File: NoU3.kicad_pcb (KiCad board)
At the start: 4 copper layers, 46 x 56 mm, 119 parts, among them J1 JST SR/SZ, J10 JST SR/SZ, J11 Screw_Terminal_01x02, J12 Screw_Terminal_01x02, J13 JST SR/SZ, J14 RFANT3216120A5T, J15 Barrel_Jack, J16 VIN, J17 JST SR/SZ, J18 GND, J19 JST SR/SZ, J2 Screw_Terminal_01x02, J3 Screw_Terminal_01x02, J4 JST SR/SZ, J5 Screw_Terminal_01x02, J6 Screw_Terminal_01x02, J7 JST SR/SZ, J8 Screw_Terminal_01x02, J9 Screw_Terminal_01x02, Q1 AO3401A, SW1 reset, SW2 boot, U1 HR8833, U10 PCA9685BS, U11 Qwiic1, U15 SY8113BADC, U16 SY8113BADC, U17 USB_C_Receptacle, U18 ServoPorts_2x3, U19 ServoPorts_2x3, U2 ESP32-S3FN8, U26 LSM6DS3TR-C, U3 Crystal_ESP32, U4 HR8833, U5 HR8833, U6 HR8833, U7 ServoPorts_2x3, U8 5.8 ZSPT, U9 USBLC6-2P6

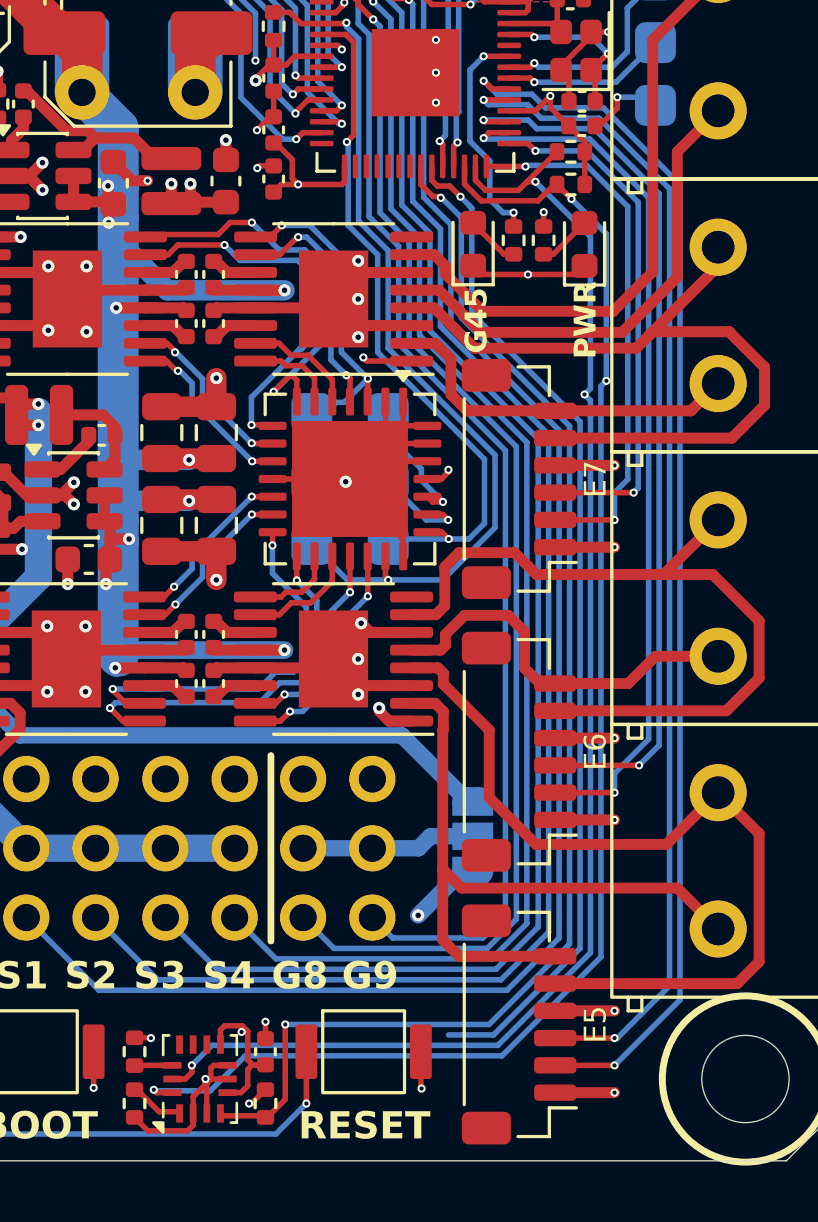
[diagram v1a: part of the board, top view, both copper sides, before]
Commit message: cleaned up JSTs on motor driver sheet
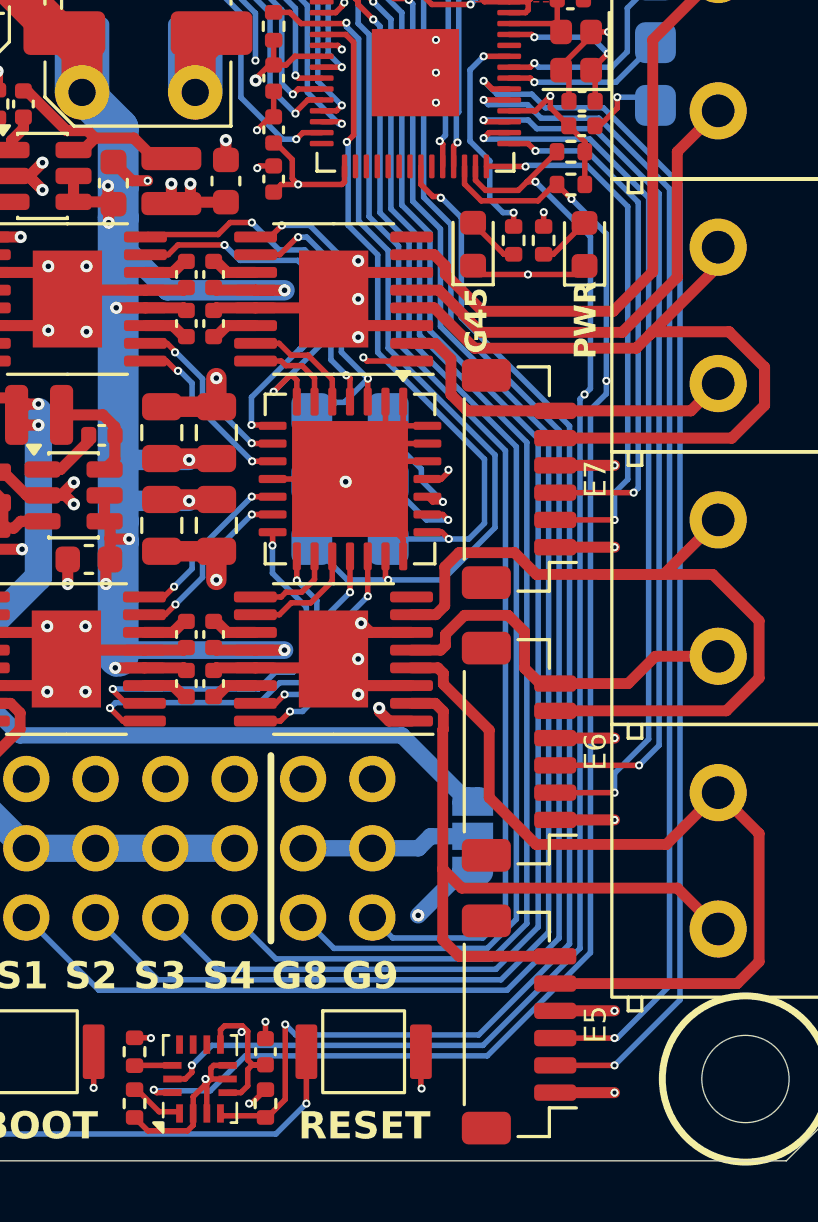
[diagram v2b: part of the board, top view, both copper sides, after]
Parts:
- C1: value 100nF -> 1uF
- R5: value 1K -> 10K
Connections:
- net /MotorSystem/MotorDriver-1/Aout1 renamed Net-(J1-Pin_6)
- net /MotorSystem/MotorDriver-1/Aout2 renamed Net-(J1-Pin_5)
- net /MotorSystem/MotorDriver-3/Aout1 renamed Net-(J7-Pin_6)
- net /MotorSystem/MotorDriver-3/Aout2 renamed Net-(J7-Pin_5)
- net /MotorSystem/MotorDriver-4/Aout1 renamed Net-(J10-Pin_6)
- net /MotorSystem/MotorDriver-4/Aout2 renamed Net-(J10-Pin_5)
- net MD2_A1 renamed Net-(J19-Pin_6)
- net MD2_A2 renamed Net-(J19-Pin_5)
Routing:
- net SF_INT1: track 37.3 -> 0.00 mm, vias 1 -> 0

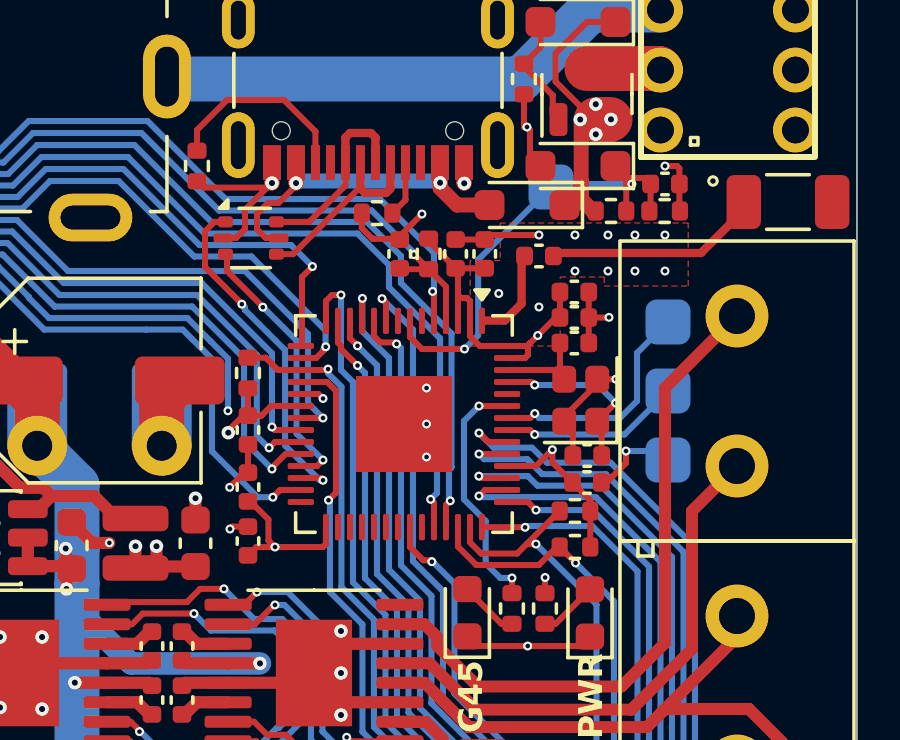
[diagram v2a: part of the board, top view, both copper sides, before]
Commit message: Reroute PCB connections and adjust DRC rules
Add and revise PCB routing for several connector and component nets, including repositioning U9. Ignore silkscreen clearance and overlap violations, and update schematic notes.
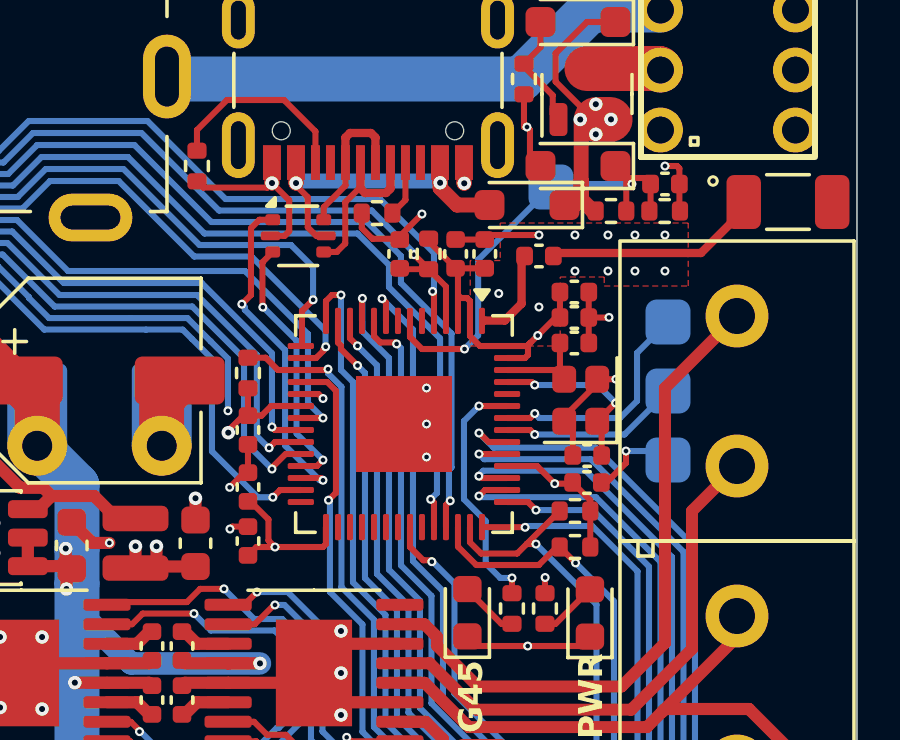
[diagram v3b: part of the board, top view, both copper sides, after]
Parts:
- moved U9 1.58 mm to (4.38, -16.2)
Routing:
- net Net-(U17-D+-PadA6): track 6.36 -> 5.00 mm
- net Net-(U17-D--PadA7): track 6.56 -> 5.73 mm
- net /VUSB: track 11.4 -> 10.6 mm
- net +3V3: track 64.3 -> 63.7 mm

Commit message: first push with NoU3.7 features
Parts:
- removed Q1: AO3401A, AlfredoFootprints:SOT-23-small
- removed R23: 10K, Resistor_SMD:R_0402_1005Metric
- removed TP4: ECLK, AlfredoFootprints:PogoPad1
- removed TP5: LED0, AlfredoFootprints:PogoPad1
- removed TP6: SCL, AlfredoFootprints:PogoPad1
- removed TP7: SDA, AlfredoFootprints:PogoPad1
- removed TP8: MOE, AlfredoFootprints:PogoPad1
- removed TP9: GND, AlfredoFootprints:PogoPad1
- removed U10: PCA9685BS, Package_DFN_QFN:QFN-28-1EP_6x6mm_P0.65mm_EP4.25x4.25mm
- added C17: 100nF, Capacitor_SMD:C_0402_1005Metric, F.Cu at (-17.3, -35.7)
- added C18: 100nF, Capacitor_SMD:C_0402_1005Metric, F.Cu at (-17.3, -33.7)
- added C39: 10uF, Capacitor_SMD:C_0402_1005Metric, F.Cu at (-17.3, -31.8)
- added D60: LED_yellow, LED_SMD:LED_0402_1005Metric, F.Cu at (-14.1, -35.7)
- added J20: JST SR/SZ, AlfredoFootprints:JST_SH_1x06_Vertical, F.Cu at (-13.3, -41.8)
- added Q2: AONR21357, Package_DFN_QFN:DFN-8-1EP_3x3mm_P0.65mm_EP1.55x2.4mm, F.Cu at (-31.4, -44.4)
- added R29: 100mR, Resistor_SMD:R_0805_2012Metric, F.Cu at (-36.9, -36.0)
- added R30: 100mR, Resistor_SMD:R_0805_2012Metric, F.Cu at (-24.1, -36.0)
- added R31: 100mR, Resistor_SMD:R_0805_2012Metric, F.Cu at (-36.9, -28.1)
- added R32: 100mR, Resistor_SMD:R_0805_2012Metric, F.Cu at (-30.5, -36.0)
- added R33: 100mR, Resistor_SMD:R_0805_2012Metric, F.Cu at (-36.9, -33.0)
- added R34: 100mR, Resistor_SMD:R_0805_2012Metric, F.Cu at (-24.1, -33.0)
- added R35: 100mR, Resistor_SMD:R_0805_2012Metric, F.Cu at (-36.4, -24.1)
- added R36: 100mR, Resistor_SMD:R_0805_2012Metric, F.Cu at (-30.5, -33.0)
- added R67: 1K, Resistor_SMD:R_0201_0603Metric, F.Cu at (-14.6, -33.8)
- added U12: PY32F003F16U6TR, Package_DFN_QFN:VQFN-20-1EP_3x3mm_P0.4mm_EP1.7x1.7mm, F.Cu at (-29.7, -26.9)
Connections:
- net /MotorSystem/MotorDriver-1/Bout1 renamed Net-(J20-Pin_6)
- net /MotorSystem/MotorDriver-1/Bout2 renamed Net-(J20-Pin_5)
- J10 pad 2: E4B -> E6A
- J12 pad 1: MD4_B1 -> Net-(J12-Pin_1)
- J12 pad 2: MD4_B2 -> Net-(J12-Pin_2)
- J13 pad 3: E5A -> E3B
- J13 pad 5: MD3_B1 -> Net-(J13-Pin_5)
- J13 pad 6: MD3_B2 -> Net-(J13-Pin_6)
- J17 pad 3: E6A -> E4B
- J17 pad 5: MD4_B1 -> Net-(J12-Pin_2)
- J17 pad 6: MD4_B2 -> Net-(J12-Pin_1)
- J19 pad 2: E7B -> E2A
- J4 pad 3: E2A -> E7B
- J4 pad 5: /MotorSystem/MotorDriver-2/Bout1 -> Net-(J4-Pin_5)
- J4 pad 6: /MotorSystem/MotorDriver-2/Bout2 -> Net-(J4-Pin_6)
- J6 pad 1: /MotorSystem/MotorDriver-2/Bout1 -> Net-(J4-Pin_6)
- J6 pad 2: /MotorSystem/MotorDriver-2/Bout2 -> Net-(J4-Pin_5)
- J7 pad 2: E3B -> E5A
- J9 pad 1: MD3_B1 -> Net-(J13-Pin_6)
- J9 pad 2: MD3_B2 -> Net-(J13-Pin_5)
- U1 pad 3: GND -> /MotorSystem/MotorDriver-1/AISEN
- U1 pad 6: GND -> /MotorSystem/MotorDriver-1/BISEN
- U4 pad 3: GND -> /MotorSystem/MotorDriver-2/AISEN
- U4 pad 5: /MotorSystem/MotorDriver-2/Bout2 -> Net-(J4-Pin_5)
- U4 pad 6: GND -> /MotorSystem/MotorDriver-2/BISEN
- U4 pad 7: /MotorSystem/MotorDriver-2/Bout1 -> Net-(J4-Pin_6)
- U5 pad 3: GND -> /MotorSystem/MotorDriver-3/AISEN
- U5 pad 5: MD3_B2 -> Net-(J13-Pin_5)
- U5 pad 6: GND -> /MotorSystem/MotorDriver-3/BISEN
- U5 pad 7: MD3_B1 -> Net-(J13-Pin_6)
- U6 pad 3: GND -> /MotorSystem/MotorDriver-4/AISEN
- U6 pad 5: MD4_B2 -> Net-(J12-Pin_2)
- U6 pad 6: GND -> /MotorSystem/MotorDriver-4/BISEN
- U6 pad 7: MD4_B1 -> Net-(J12-Pin_1)
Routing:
- net (no net): track 0.00 -> 146.0 mm, vias 0 -> 2
- net MD4_B1: track 30.8 -> 0.00 mm
- net /MotorSystem/MotorDriver-2/Bout2: track 28.8 -> 0.00 mm
- net MD3_B2: track 28.1 -> 0.00 mm, vias 2 -> 0
- net MD3_B1: track 25.6 -> 0.00 mm
- net GND: track 148.6 -> 128.2 mm, vias 68 -> 67
- net /MotorSystem/MotorDriver-2/Bout1: track 17.8 -> 0.00 mm
- net MD4_B2: track 14.9 -> 0.00 mm
- net /MotorSystem/MotorDriver-2/AIN1: track 14.6 -> 0.00 mm, vias 2 -> 0
- net /MotorSystem/MotorDriver-3/BIN2: track 14.1 -> 0.00 mm, vias 2 -> 0
- net /MotorSystem/MotorDriver-3/BIN1: track 14.0 -> 0.00 mm, vias 2 -> 0
- net /MotorSystem/MotorDriver-2/AIN2: track 13.9 -> 0.00 mm, vias 2 -> 0
- net /MotorSystem/MotorDriver-1/BIN1: track 12.1 -> 0.00 mm, vias 2 -> 0
- net VCC: track 120.2 -> 110.2 mm, vias 14 -> 10
- net /MotorSystem/MotorDriver-1/BIN2: track 8.67 -> 0.00 mm, vias 2 -> 0
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
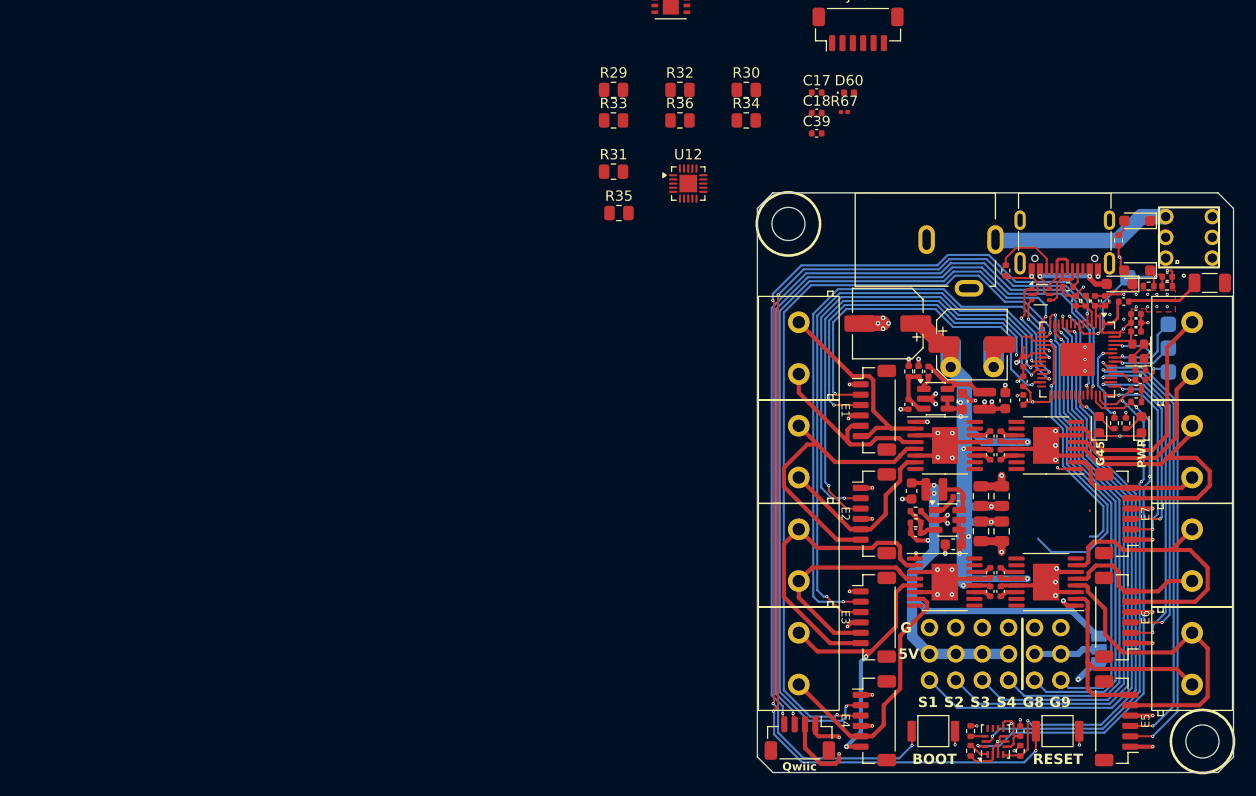
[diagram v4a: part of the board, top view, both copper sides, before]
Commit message: PY32F030K28U6TR motor controller chip
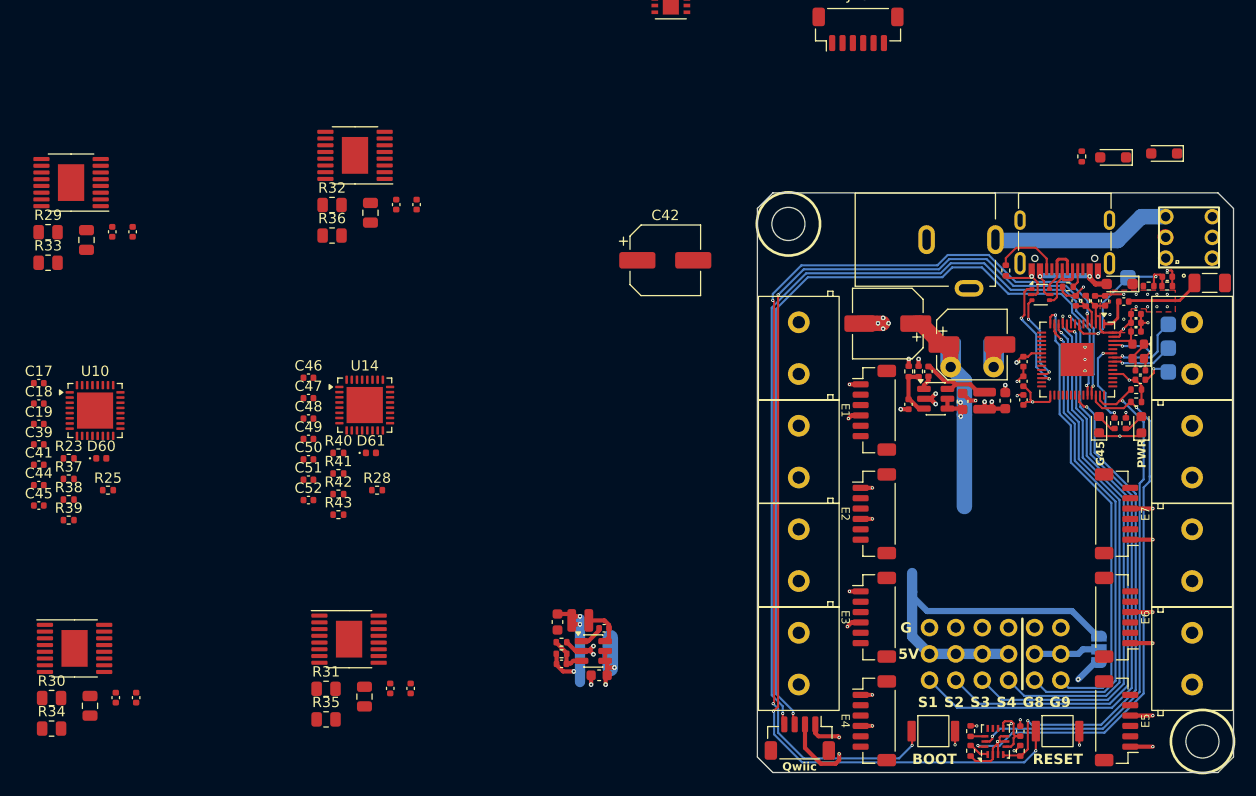
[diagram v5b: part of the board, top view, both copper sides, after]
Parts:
- removed R67: 1K, Resistor_SMD:R_0201_0603Metric
- removed U12: PY32F003F16U6TR, Package_DFN_QFN:VQFN-20-1EP_3x3mm_P0.4mm_EP1.7x1.7mm
- added C19: 1nF, Capacitor_SMD:C_0402_1005Metric, F.Cu at (-92.4, -3.67)
- added C41: 1nF, Capacitor_SMD:C_0402_1005Metric, F.Cu at (-92.4, 0.27)
- added C42: 220uF, Capacitor_SMD:CP_Elec_6.3x7.7, F.Cu at (-31.9, -19.5)
- added C44: 1nF, Capacitor_SMD:C_0402_1005Metric, F.Cu at (-92.4, 2.23)
- added C45: 1nF, Capacitor_SMD:C_0402_1005Metric, F.Cu at (-92.4, 4.21)
- added C46: 100nF, Capacitor_SMD:C_0402_1005Metric, F.Cu at (-66.4, -8.14)
- added C47: 10uF, Capacitor_SMD:C_0402_1005Metric, F.Cu at (-66.4, -6.17)
- added C48: 100nF, Capacitor_SMD:C_0402_1005Metric, F.Cu at (-66.4, -4.20)
- added C49: 1nF, Capacitor_SMD:C_0402_1005Metric, F.Cu at (-66.4, -2.23)
- added C50: 1nF, Capacitor_SMD:C_0402_1005Metric, F.Cu at (-66.4, -0.26)
- added C51: 1nF, Capacitor_SMD:C_0402_1005Metric, F.Cu at (-66.4, 1.71)
- added C52: 1nF, Capacitor_SMD:C_0402_1005Metric, F.Cu at (-66.4, 3.68)
- added D61: LED_yellow, LED_SMD:LED_0402_1005Metric, F.Cu at (-60.3, -0.88)
- added R23: 1K, Resistor_SMD:R_0402_1005Metric, F.Cu at (-89.5, -0.35)
- added R25: 1K, Resistor_SMD:R_0402_1005Metric, F.Cu at (-85.7, 2.72)
- added R28: 1K, Resistor_SMD:R_0402_1005Metric, F.Cu at (-59.7, 2.72)
- added R37: 1K, Resistor_SMD:R_0402_1005Metric, F.Cu at (-89.5, 1.64)
- added R38: 1K, Resistor_SMD:R_0402_1005Metric, F.Cu at (-89.5, 3.62)
- added R39: 1K, Resistor_SMD:R_0402_1005Metric, F.Cu at (-89.5, 5.62)
- added R40: 1K, Resistor_SMD:R_0402_1005Metric, F.Cu at (-63.5, -0.88)
- added R41: 1K, Resistor_SMD:R_0402_1005Metric, F.Cu at (-63.5, 1.11)
- added R42: 1K, Resistor_SMD:R_0402_1005Metric, F.Cu at (-63.5, 3.10)
- added R43: 1K, Resistor_SMD:R_0402_1005Metric, F.Cu at (-63.5, 5.09)
- added U10: PY32F030K28U6TR, Package_DFN_QFN:VQFN-32-1EP_5x5mm_P0.5mm_EP3.5x3.5mm, F.Cu at (-87.0, -4.97)
- added U14: PY32F030K28U6TR, Package_DFN_QFN:VQFN-32-1EP_5x5mm_P0.5mm_EP3.5x3.5mm, F.Cu at (-60.9, -5.50)
- moved U1 97.6 mm to (-89.3, -27.0)
- moved C2 90.9 mm to (-87.8, -21.4)
- moved C5 89.7 mm to (-87.5, 23.6)
- moved R30 89.2 mm to (-91.2, 22.8)
- moved R34 89.2 mm to (-91.2, 25.8)
- moved C3 88.1 mm to (-85.3, -22.2)
- moved C6 87.7 mm to (-85.0, 22.8)
- moved C4 86.6 mm to (-83.4, -22.2)
- moved U4 86.4 mm to (-89.0, 18.0)
- moved C7 86.3 mm to (-83.0, 22.8)
- moved C39 80.9 mm to (-92.4, -1.71)
- moved D60 80.4 mm to (-86.4, -0.35)
- moved C17 80.2 mm to (-92.4, -7.62)
- moved C18 80.2 mm to (-92.4, -5.64)
- moved U6 78.5 mm to (-61.9, -29.6)
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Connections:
- net /MotorSystem/MotorDriver-1/AISEN renamed /MotorSystem/MotorDriver-1/SENSEI_1
- net /MotorSystem/MotorDriver-1/BISEN renamed /MotorSystem/MotorDriver-1/SENSEI_2
- net /MotorSystem/MotorDriver-2/AISEN renamed /MotorSystem/MotorDriver-2/SENSEI_1
- net /MotorSystem/MotorDriver-2/BISEN renamed /MotorSystem/MotorDriver-2/SENSEI_2
- net /MotorSystem/MotorDriver-3/AISEN renamed /MotorSystem/MotorDriver-3/SENSEI_1
- net /MotorSystem/MotorDriver-3/BISEN renamed /MotorSystem/MotorDriver-3/SENSEI_2
- net /MotorSystem/MotorDriver-4/AISEN renamed /MotorSystem/MotorDriver-4/SENSEI_1
- net /MotorSystem/MotorDriver-4/BISEN renamed /MotorSystem/MotorDriver-4/SENSEI_2
- C18 pad 1: /MotorSystem/NoU3-MotorMCU/MOTOR_NRST -> MOTOR_PY_NRST
- J1 pad 2: E1B -> E7B
- J1 pad 3: E1A -> E7A
- J10 pad 2: E6A -> E5B
- J10 pad 3: E4A -> E5A
- J13 pad 2: E5B -> E4B
- J13 pad 3: E3B -> E4A
- J17 pad 3: E4B -> E6A
- J19 pad 2: E2A -> E1B
- J19 pad 3: E7A -> E1A
- J4 pad 3: E7B -> E2A
- J7 pad 2: E5A -> E3B
- U1 pad 10: /MotorSystem/MotorDriver-1/BIN2 -> /MotorSystem/MotorDriver-1/MOTOR_SIGNAL_2A
- U1 pad 15: /MotorSystem/MotorDriver-1/AIN2 -> /MotorSystem/MotorDriver-1/MOTOR_SIGNAL_1B
- U1 pad 16: /MotorSystem/MotorDriver-1/AIN1 -> /MotorSystem/MotorDriver-1/MOTOR_SIGNAL_1A
- U1 pad 2: Net-(J1-Pin_6) -> Net-(J19-Pin_6)
- U1 pad 4: Net-(J1-Pin_5) -> Net-(J19-Pin_5)
- U1 pad 5: Net-(J20-Pin_5) -> Net-(J4-Pin_5)
- U1 pad 7: Net-(J20-Pin_6) -> Net-(J4-Pin_6)
- U1 pad 9: /MotorSystem/MotorDriver-1/BIN1 -> /MotorSystem/MotorDriver-1/MOTOR_SIGNAL_2B
- U2 pad 15: E5B -> unconnected-(U2-GPIO10-Pad15)
- U2 pad 16: E5A -> unconnected-(U2-GPIO11-Pad16)
- U2 pad 17: M_OE -> unconnected-(U2-GPIO12-Pad17)
- U2 pad 18: M_ECLK -> unconnected-(U2-GPIO13-Pad18)
- U2 pad 19: E7A -> unconnected-(U2-GPIO14-Pad19)
- U2 pad 21: E3B -> unconnected-(U2-XTAL32K_P-Pad21)
- U2 pad 22: E3A -> unconnected-(U2-XTAL_32K_N-Pad22)
- U2 pad 23: E2B -> unconnected-(U2-GPIO17/DAC_1-Pad23)
- U2 pad 24: E2A -> unconnected-(U2-GPIO18/DAC_2-Pad24)
- U2 pad 27: E7B -> unconnected-(U2-GPIO21-Pad27)
- U2 pad 37: SF_INT1 -> unconnected-(U2-SPICLK_P-Pad37)
- U2 pad 42: E1B -> unconnected-(U2-GPIO37-Pad42)
- U2 pad 43: E1A -> unconnected-(U2-GPIO38-Pad43)
- U2 pad 44: E6B -> unconnected-(U2-MTCK-Pad44)
- U2 pad 45: E6A -> unconnected-(U2-MTDO-Pad45)
- U2 pad 47: E4A -> unconnected-(U2-MTDI-Pad47)
- U2 pad 48: E4B -> unconnected-(U2-MTMS-Pad48)
- U4 pad 10: /MotorSystem/MotorDriver-2/BIN2 -> /MotorSystem/MotorDriver-2/MOTOR_SIGNAL_2A
- U4 pad 15: /MotorSystem/MotorDriver-2/AIN2 -> /MotorSystem/MotorDriver-2/MOTOR_SIGNAL_1B
- U4 pad 16: /MotorSystem/MotorDriver-2/AIN1 -> /MotorSystem/MotorDriver-2/MOTOR_SIGNAL_1A
- U4 pad 2: Net-(J19-Pin_6) -> Net-(J7-Pin_6)
- U4 pad 4: Net-(J19-Pin_5) -> Net-(J7-Pin_5)
- U4 pad 5: Net-(J4-Pin_5) -> Net-(J13-Pin_5)
- U4 pad 7: Net-(J4-Pin_6) -> Net-(J13-Pin_6)
- U4 pad 9: /MotorSystem/MotorDriver-2/BIN1 -> /MotorSystem/MotorDriver-2/MOTOR_SIGNAL_2B
- U5 pad 10: /MotorSystem/MotorDriver-3/BIN2 -> /MotorSystem/MotorDriver-3/MOTOR_SIGNAL_2A
- U5 pad 15: /MotorSystem/MotorDriver-3/AIN2 -> /MotorSystem/MotorDriver-3/MOTOR_SIGNAL_1B
- U5 pad 16: /MotorSystem/MotorDriver-3/AIN1 -> /MotorSystem/MotorDriver-3/MOTOR_SIGNAL_1A
- U5 pad 2: Net-(J7-Pin_6) -> Net-(J10-Pin_6)
- U5 pad 4: Net-(J7-Pin_5) -> Net-(J10-Pin_5)
- U5 pad 5: Net-(J13-Pin_5) -> Net-(J12-Pin_2)
- U5 pad 7: Net-(J13-Pin_6) -> Net-(J12-Pin_1)
- U5 pad 9: /MotorSystem/MotorDriver-3/BIN1 -> /MotorSystem/MotorDriver-3/MOTOR_SIGNAL_2B
- U6 pad 10: /MotorSystem/MotorDriver-4/BIN2 -> /MotorSystem/MotorDriver-4/MOTOR_SIGNAL_2A
- U6 pad 15: /MotorSystem/MotorDriver-4/AIN2 -> /MotorSystem/MotorDriver-4/MOTOR_SIGNAL_1B
- U6 pad 16: /MotorSystem/MotorDriver-4/AIN1 -> /MotorSystem/MotorDriver-4/MOTOR_SIGNAL_1A
- U6 pad 2: Net-(J10-Pin_6) -> Net-(J1-Pin_6)
- U6 pad 4: Net-(J10-Pin_5) -> Net-(J1-Pin_5)
- U6 pad 5: Net-(J12-Pin_2) -> Net-(J20-Pin_5)
- U6 pad 7: Net-(J12-Pin_1) -> Net-(J20-Pin_6)
- U6 pad 9: /MotorSystem/MotorDriver-4/BIN1 -> /MotorSystem/MotorDriver-4/MOTOR_SIGNAL_2B
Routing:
- net (no net): track 146.0 -> 0.00 mm, vias 2 -> 0
- net E5B: track 78.4 -> 0.00 mm, vias 2 -> 0
- net E5A: track 75.9 -> 0.00 mm, vias 2 -> 0
- net E3B: track 60.7 -> 0.00 mm, vias 2 -> 0
- net E3A: track 58.4 -> 0.00 mm, vias 2 -> 0
- net GND: track 128.2 -> 77.0 mm, vias 67 -> 49
- net E2B: track 47.3 -> 0.00 mm, vias 2 -> 0
- net E2A: track 47.0 -> 0.00 mm, vias 2 -> 0
- net E4B: track 45.3 -> 0.00 mm, vias 2 -> 0
- net E4A: track 43.3 -> 0.00 mm, vias 2 -> 0
- net VCC: track 110.2 -> 72.8 mm, vias 10 -> 4
- net E7A: track 36.9 -> 0.00 mm, vias 3 -> 0
- net E7B: track 35.1 -> 0.00 mm, vias 2 -> 0
- net E6A: track 33.0 -> 0.00 mm, vias 2 -> 0
- net E6B: track 32.5 -> 0.00 mm, vias 2 -> 0
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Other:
- board text removed: "ECLK"
- board text removed: "LED0"
- board text removed: "MOE"
- board text removed: "SCL"
- board text removed: "SDA"
